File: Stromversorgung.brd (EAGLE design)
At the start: 80 x 100 mm, 16 parts, among them J1 DCJ0202, U1 TSR 2-2450, U2 TSR 1-2433, U3 TSR 2-2450, X1 Ein/Aus, X2 MAC64L

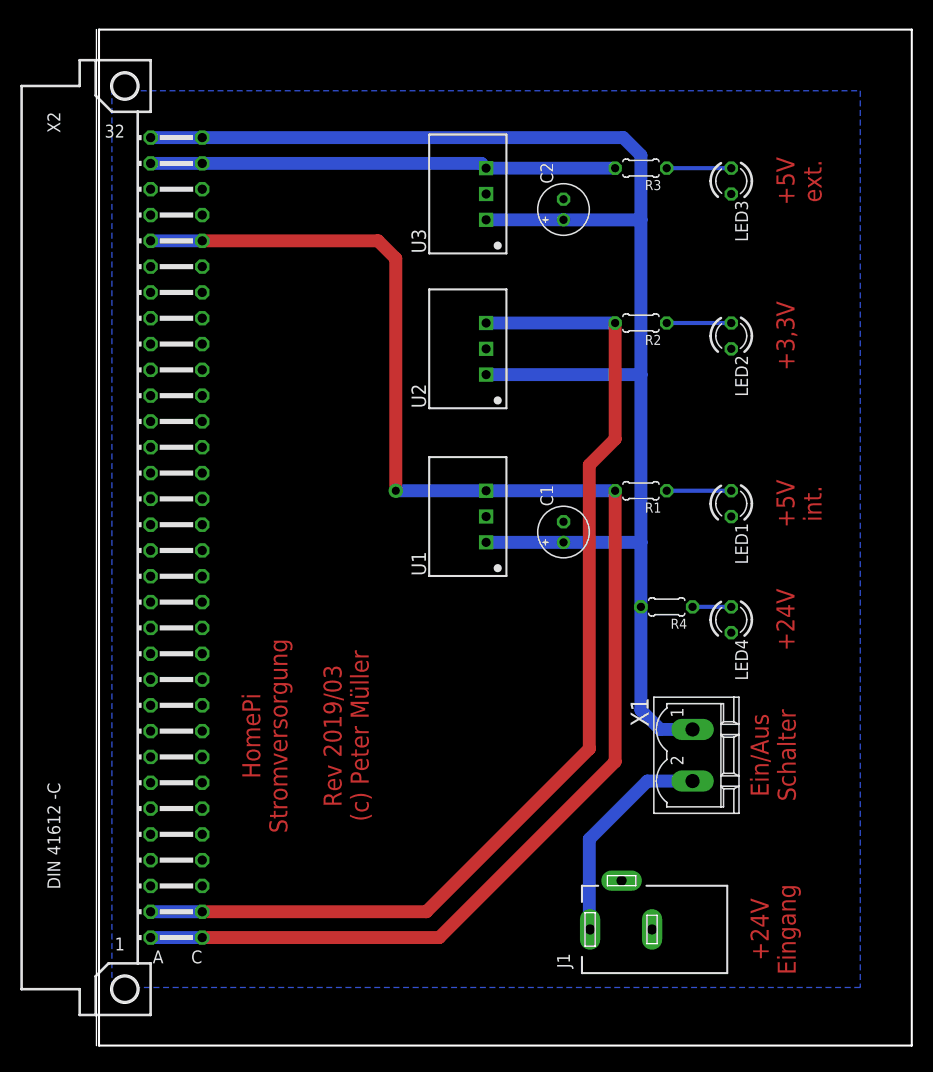
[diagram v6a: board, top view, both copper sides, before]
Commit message: Pi, CanBus, Stromversorgung, Steckverbinder angepasst
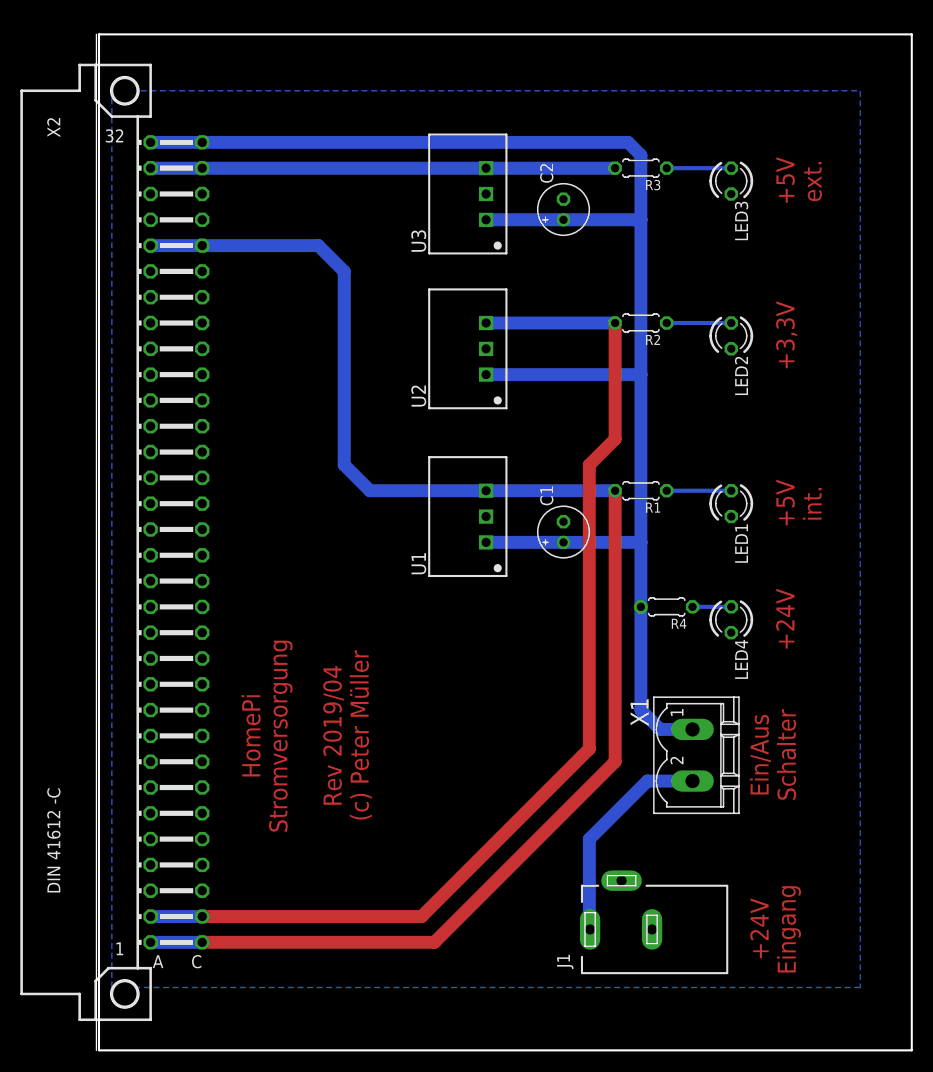
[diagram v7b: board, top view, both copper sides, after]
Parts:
- moved X2 0.47 mm to (2.54, 49.5)
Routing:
- net +5V_INT: track 148.9 -> 146.6 mm, vias 1 -> 0
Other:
- board text added: "HomePi Stromversorgung Rev 2019/04 (c) Peter Müller"
- board text removed: "HomePi Stromversorgung Rev 2019/03 (c) Peter Müller"
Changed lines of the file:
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@@
 <board>
 <plain>
-<wire x1="0" y1="0" x2="80" y2="0" width="0.2" layer="20"/>
-<wire x1="80" y1="0" x2="80" y2="100" width="0.2" layer="20"/>
-<wire x1="80" y1="100" x2="0" y2="100" width="0.2" layer="20"/>
-<wire x1="0" y1="100" x2="0" y2="0" width="0.2" layer="20"/>
+<wire x1="0" y1="-0.47" x2="80" y2="-0.47" width="0.2" layer="20"/>
+<wire x1="80" y1="-0.47" x2="80" y2="99.53" width="0.2" layer="20"/>
+<wire x1="80" y1="99.53" x2="0" y2="99.53" width="0.2" layer="20"/>
+<wire x1="0" y1="99.53" x2="0" y2="-0.47" width="0.2" layer="20"/>
 <text x="64.135" y="11.43" size="1.778" layer="1" font="vector" ratio="15" rot="R90" align="top-center">+24V
 Eingang</text>
 <text x="20.32" y="30.48" size="1.778" layer="1" font="vector" ratio="15" rot="R90" align="center">HomePi
 Stromversorgung
-Rev 2019/03
+Rev 2019/04
 (c) Peter Müller</text>
 <text x="66.675" y="53.34" size="1.778" layer="1" font="vector" ratio="15" rot="R90" align="top-center">+5V
@@
 <attribute name="MF" value="" x="51.435" y="11.43" size="1.778" layer="27" rot="R90" display="off"/>
 </element>
-<element name="X2" library="con-vg" package="MAC64L" value="MAC64L" x="2.54" y="50" rot="R180"/>
+<element name="X2" library="con-vg" package="MAC64L" value="MAC64L" x="2.54" y="49.53" locked="yes" rot="R180"/>
 <element name="C1" library="rcl" package="E2-5" value="22µF 50V Low-ESR" x="45.72" y="50.545" rot="R90"/>
 <element name="C2" library="rcl" package="E2-5" value="22µF 50V Low-ESR" x="45.72" y="82.292" rot="R90"/>
@@
 <contactref element="X2" pad="C28"/>
 <wire x1="38.1" y1="54.61" x2="50.8" y2="54.61" width="1.27" layer="16"/>
-<wire x1="10.16" y1="10.63" x2="33.49" y2="10.63" width="1.27" layer="1"/>
-<wire x1="33.49" y1="10.63" x2="50.8" y2="27.94" width="1.27" layer="1"/>
 <wire x1="50.8" y1="27.94" x2="50.8" y2="54.61" width="1.27" layer="1"/>
-<wire x1="5.08" y1="10.63" x2="10.16" y2="10.63" width="1.27" layer="16"/>
-<wire x1="10.16" y1="79.21" x2="27.47" y2="79.21" width="1.27" layer="1"/>
-<wire x1="27.47" y1="79.21" x2="29.21" y2="77.47" width="1.27" layer="1"/>
-<wire x1="38.1" y1="54.61" x2="29.21" y2="54.61" width="1.27" layer="16"/>
-<via x="29.21" y="54.61" extent="1-16" drill="0.8" diameter="1.4224"/>
-<wire x1="29.21" y1="54.61" x2="29.21" y2="77.47" width="1.27" layer="1"/>
-<wire x1="5.08" y1="79.21" x2="10.16" y2="79.21" width="1.27" layer="16"/>
+<wire x1="5.08" y1="10.16" x2="10.16" y2="10.16" width="1.27" layer="16"/>
+<wire x1="5.08" y1="78.74" x2="10.16" y2="78.74" width="1.27" layer="16"/>
+<wire x1="10.16" y1="10.16" x2="33.02" y2="10.16" width="1.27" layer="1"/>
+<wire x1="33.02" y1="10.16" x2="50.8" y2="27.94" width="1.27" layer="1"/>
+<wire x1="38.1" y1="54.61" x2="26.67" y2="54.61" width="1.27" layer="16"/>
+<wire x1="26.67" y1="54.61" x2="24.13" y2="57.15" width="1.27" layer="16"/>
+<wire x1="24.13" y1="57.15" x2="24.13" y2="76.2" width="1.27" layer="16"/>
+<wire x1="24.13" y1="76.2" x2="21.59" y2="78.74" width="1.27" layer="16"/>
+<wire x1="21.59" y1="78.74" x2="10.16" y2="78.74" width="1.27" layer="16"/>
 </signal>
 <signal name="+5V_EXT">
@@
 <contactref element="X2" pad="A31"/>
 <contactref element="X2" pad="C31"/>
-<wire x1="10.16" y1="86.83" x2="5.08" y2="86.83" width="1.27" layer="16"/>
+<wire x1="10.16" y1="86.36" x2="5.08" y2="86.36" width="1.27" layer="16"/>
 <wire x1="38.1" y1="86.36" x2="50.8" y2="86.36" width="1.27" layer="16"/>
-<wire x1="10.16" y1="86.83" x2="37.63" y2="86.83" width="1.27" layer="16"/>
-<wire x1="37.63" y1="86.83" x2="38.1" y2="86.36" width="1.27" layer="16"/>
+<wire x1="38.1" y1="86.36" x2="10.16" y2="86.36" width="1.27" layer="16"/>
 </signal>
 <signal name="+3,3V">
@@
 <wire x1="50.8" y1="71.12" x2="50.8" y2="59.69" width="1.27" layer="1"/>
 <wire x1="50.8" y1="59.69" x2="48.26" y2="57.15" width="1.27" layer="1"/>
-<wire x1="10.16" y1="13.17" x2="32.22" y2="13.17" width="1.27" layer="1"/>
-<wire x1="32.22" y1="13.17" x2="48.26" y2="29.21" width="1.27" layer="1"/>
 <wire x1="48.26" y1="57.15" x2="48.26" y2="29.21" width="1.27" layer="1"/>
-<wire x1="10.16" y1="13.17" x2="5.08" y2="13.17" width="1.27" layer="16"/>
+<wire x1="10.16" y1="12.7" x2="5.08" y2="12.7" width="1.27" layer="16"/>
 <contactref element="U2" pad="3"/>
 <wire x1="38.1" y1="71.12" x2="50.8" y2="71.12" width="1.27" layer="16"/>
+<wire x1="10.16" y1="12.7" x2="31.75" y2="12.7" width="1.27" layer="1"/>
+<wire x1="31.75" y1="12.7" x2="48.26" y2="29.21" width="1.27" layer="1"/>
 </signal>
 <signal name="N$6">
@@
 <wire x1="53.34" y1="49.529" x2="53.34" y2="66.04" width="1.27" layer="16"/>
 <wire x1="53.34" y1="66.04" x2="53.34" y2="81.276" width="1.27" layer="16"/>
-<wire x1="53.34" y1="81.276" x2="53.34" y2="87.63" width="1.27" layer="16"/>
-<wire x1="10.16" y1="89.37" x2="51.6" y2="89.37" width="1.27" layer="16"/>
-<wire x1="51.6" y1="89.37" x2="53.34" y2="87.63" width="1.27" layer="16"/>
 <contactref element="X1" pad="1"/>
 <wire x1="58.42" y1="31.115" x2="55.245" y2="31.115" width="1.27" layer="16"/>
@@
 <wire x1="45.72" y1="49.53" x2="45.72" y2="49.529" width="0.8128" layer="16"/>
 <wire x1="45.72" y1="49.529" x2="53.34" y2="49.529" width="1.27" layer="16"/>
-<wire x1="5.08" y1="89.37" x2="10.16" y2="89.37" width="1.27" layer="16"/>
+<wire x1="5.08" y1="88.9" x2="10.16" y2="88.9" width="1.27" layer="16"/>
 <contactref element="R4" pad="2"/>
 <wire x1="53.34" y1="49.529" x2="53.34" y2="43.18" width="1.27" layer="16"/>
@@
 <contactref element="U2" pad="1"/>
 <wire x1="38.1" y1="66.04" x2="53.34" y2="66.04" width="1.27" layer="16"/>
+<wire x1="53.34" y1="81.276" x2="53.34" y2="87.63" width="1.27" layer="16"/>
+<wire x1="53.34" y1="87.63" x2="52.07" y2="88.9" width="1.27" layer="16"/>
+<wire x1="52.07" y1="88.9" x2="10.16" y2="88.9" width="1.27" layer="16"/>
 </signal>
 <signal name="GND">

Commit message: Platinen angepasst, Backplane
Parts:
- moved R2 3.18 mm to (53.3, 67.9)
- moved LED2 3.17 mm to (62.2, 66.7)
- moved U2 3.17 mm to (38.1, 65.4)
- moved C2 2.54 mm to (45.7, 79.8)
- moved LED1 2.54 mm to (62.2, 50.8)
- moved LED3 2.54 mm to (62.2, 82.5)
- moved R3 2.54 mm to (53.3, 83.8)
- moved C1 2.54 mm to (45.7, 48.0)
- moved LED4 2.54 mm to (62.2, 39.4)
- moved R1 2.54 mm to (53.3, 52.1)
- moved R4 2.54 mm to (55.9, 40.6)
- moved U1 2.54 mm to (38.1, 49.5)
- moved X1 2.54 mm to (58.4, 26.0)
- moved U3 2.54 mm to (38.1, 81.3)
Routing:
- net +3,3V: track 105.7 -> 102.5 mm
- net +24V: track 155.0 -> 157.5 mm
- net N$1: track 21.4 -> 18.9 mm
- net +5V_EXT: track 45.7 -> 46.8 mm
